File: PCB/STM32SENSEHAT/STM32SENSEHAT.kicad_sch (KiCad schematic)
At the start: 0 parts

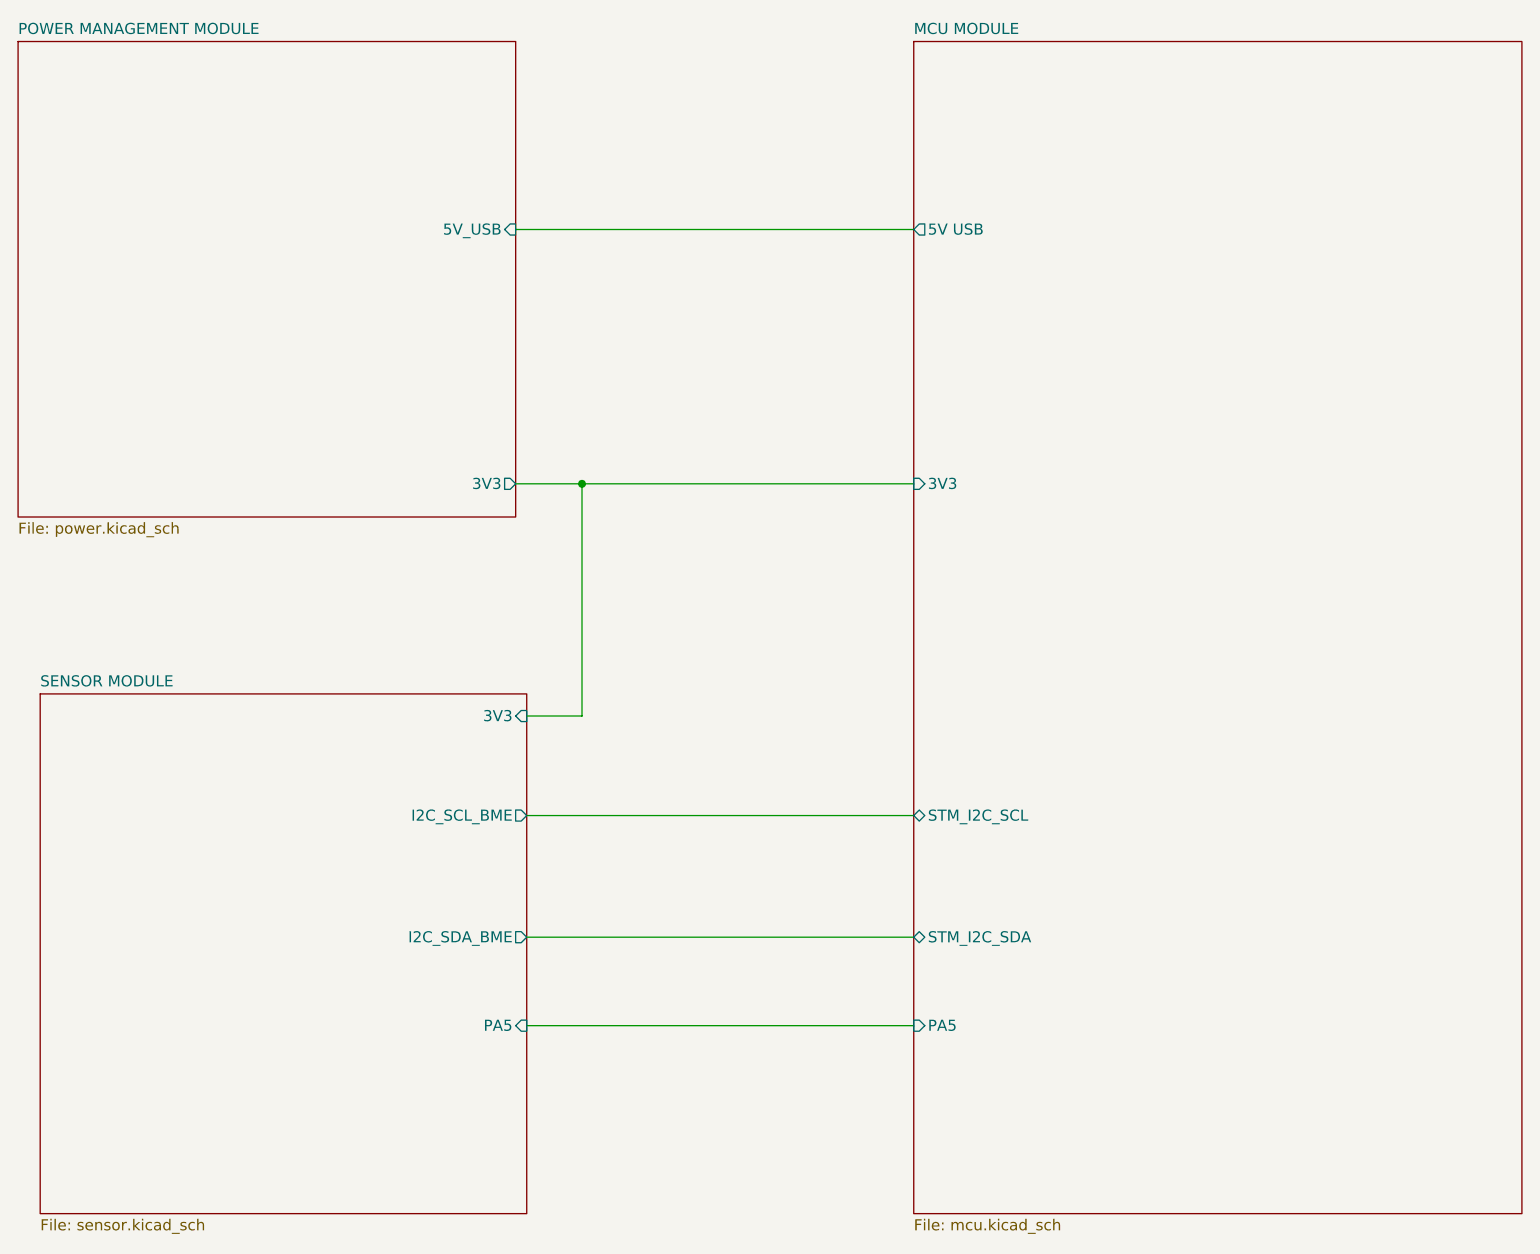
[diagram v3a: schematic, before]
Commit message: Added I2C,GPIO ports for the back up sesnors to the top level sheet
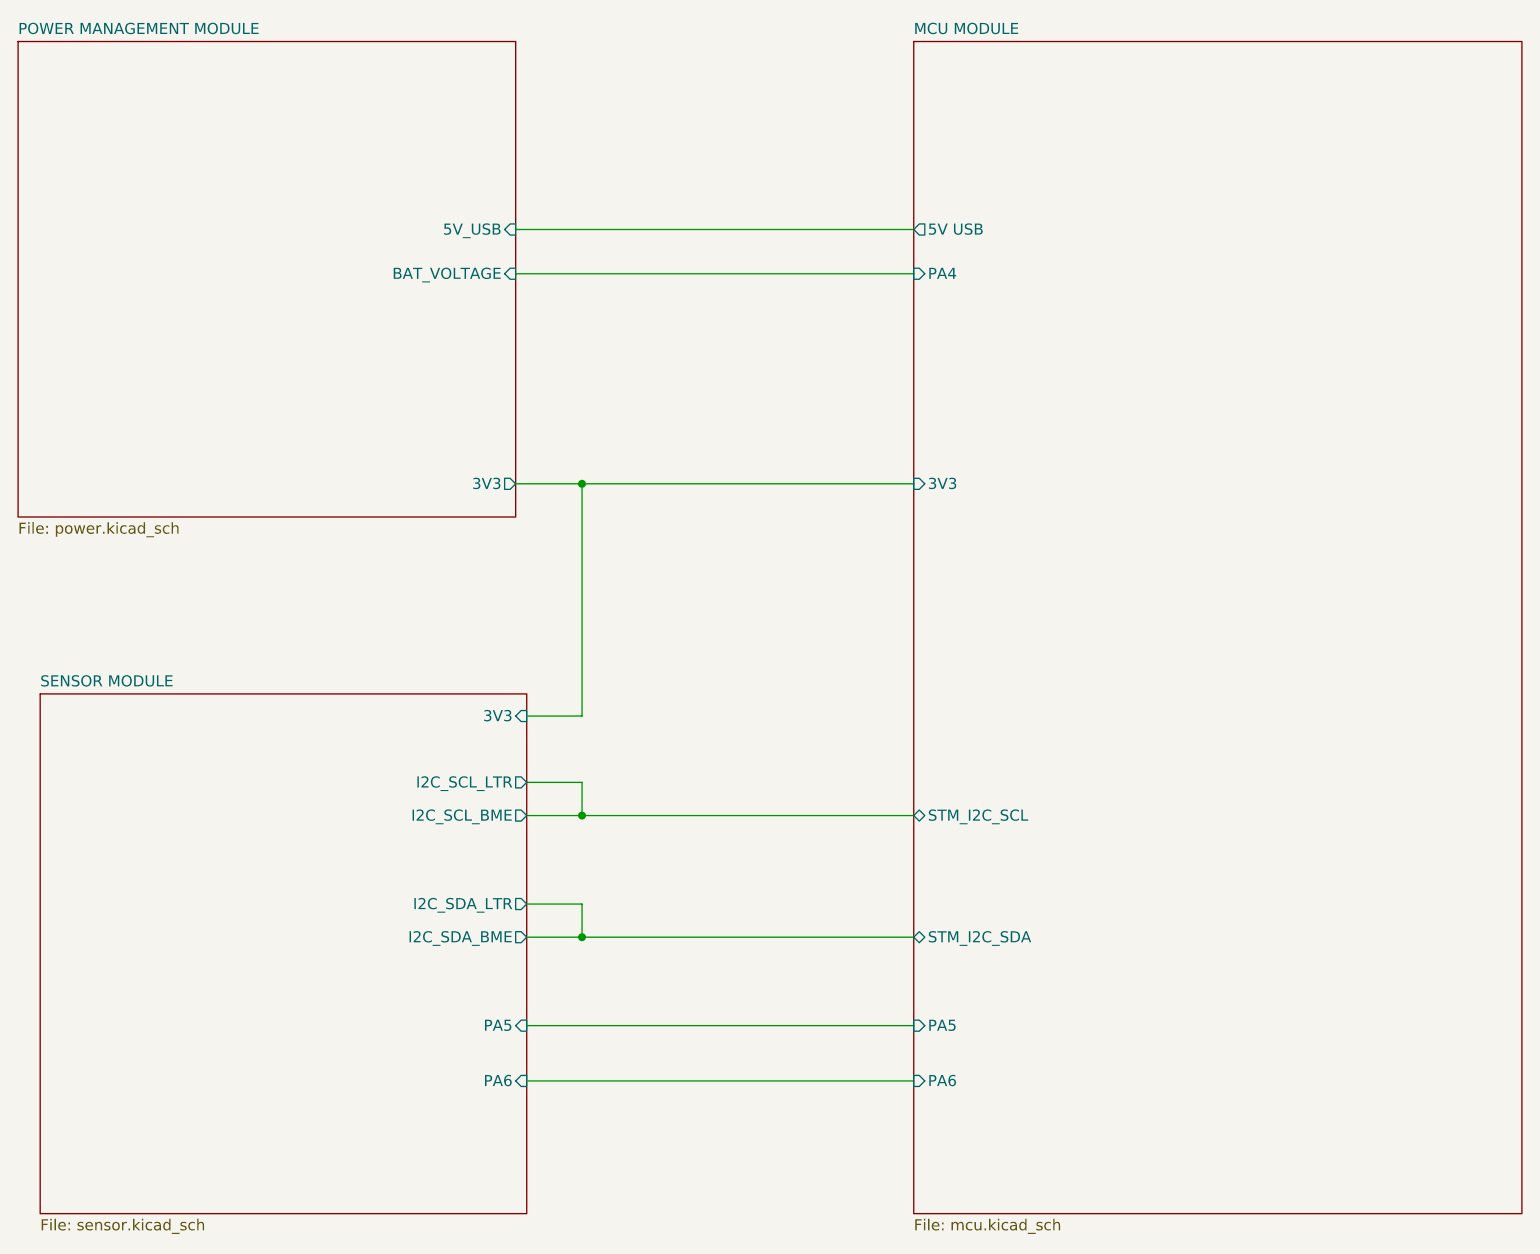
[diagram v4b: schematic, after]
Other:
- sheet MCU MODULE ports: added PA4, PA6; removed none
- sheet POWER MANAGEMENT MODULE ports: added BAT_VOLTAGE; removed none
- sheet SENSOR MODULE ports: added I2C_SCL_LTR, I2C_SDA_LTR, PA6; removed none
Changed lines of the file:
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@@
   (junction (at 99.06 73.66) (diameter 0) (color 0 0 0 0)
   )
+  (junction (at 99.06 125.73) (diameter 0) (color 0 0 0 0)
+  )
+  (junction (at 99.06 111.76) (diameter 0) (color 0 0 0 0)
+  )
+  (wire (pts (xy 92.71 142.24) (xy 137.16 142.24))
+    (stroke (width 0) (type default))
+  )
+  (wire (pts (xy 92.71 107.95) (xy 99.06 107.95))
+    (stroke (width 0) (type default))
+  )
+  (wire (pts (xy 99.06 111.76) (xy 137.16 111.76))
+    (stroke (width 0) (type default))
+  )
   (wire (pts (xy 91.44 73.66) (xy 99.06 73.66))
     (stroke (width 0) (type default))
@@
     (stroke (width 0) (type default))
   )
+  (wire (pts (xy 99.06 107.95) (xy 99.06 111.76))
+    (stroke (width 0) (type default))
+  )
   (wire (pts (xy 91.44 44.45) (xy 137.16 44.45))
     (stroke (width 0) (type default))
   )
-  (wire (pts (xy 92.71 125.73) (xy 137.16 125.73))
+  (wire (pts (xy 92.71 125.73) (xy 99.06 125.73))
+    (stroke (width 0) (type default))
+  )
+  (wire (pts (xy 99.06 121.92) (xy 99.06 125.73))
     (stroke (width 0) (type default))
   )
@@
     (stroke (width 0) (type default))
   )
-  (wire (pts (xy 92.71 111.76) (xy 137.16 111.76))
+  (wire (pts (xy 91.44 49.53) (xy 137.16 49.53))
+    (stroke (width 0) (type default))
+  )
+  (wire (pts (xy 92.71 111.76) (xy 99.06 111.76))
+    (stroke (width 0) (type default))
+  )
+  (wire (pts (xy 99.06 125.73) (xy 137.16 125.73))
+    (stroke (width 0) (type default))
+  )
+  (wire (pts (xy 92.71 121.92) (xy 99.06 121.92))
     (stroke (width 0) (type default))
   )
@@
       (effects (font (size 1.27 1.27)) (justify right))
     )
+    (pin "PA6" input (at 92.71 142.24 0)
+      (effects (font (size 1.27 1.27)) (justify right))
+    )
+    (pin "I2C_SCL_LTR" output (at 92.71 107.95 0)
+      (effects (font (size 1.27 1.27)) (justify right))
+    )
+    (pin "I2C_SDA_LTR" output (at 92.71 121.92 0)
+      (effects (font (size 1.27 1.27)) (justify right))
+    )
     (instances
       (project "STM32SENSEHAT"
@@
       (effects (font (size 1.27 1.27)) (justify left))
     )
+    (pin "PA6" input (at 137.16 142.24 180)
+      (effects (font (size 1.27 1.27)) (justify left))
+    )
+    (pin "PA4" input (at 137.16 49.53 180)
+      (effects (font (size 1.27 1.27)) (justify left))
+    )
     (instances
       (project "STM32SENSEHAT"
@@
       (effects (font (size 1.27 1.27)) (justify right))
     )
+    (pin "BAT_VOLTAGE" input (at 91.44 49.53 0)
+      (effects (font (size 1.27 1.27)) (justify right))
+    )

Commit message: Protectuion features added to all schematica
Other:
- sheet MCU MODULE ports: added none; removed 3V3, 5V USB, PA6
- sheet POWER MANAGEMENT MODULE ports: added none; removed 3V3, 5V_USB
- sheet SENSOR MODULE ports: added none; removed 3V3, PA6
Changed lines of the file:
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@@
     (comment 4 "AUTHOR(S)")
   )
-  (junction (at 99.06 73.66) (diameter 0) (color 0 0 0 0)
-  )
   (junction (at 99.06 125.73) (diameter 0) (color 0 0 0 0)
   )
   (junction (at 99.06 111.76) (diameter 0) (color 0 0 0 0)
-  )
-  (wire (pts (xy 92.71 142.24) (xy 137.16 142.24))
-    (stroke (width 0) (type default))
   )
   (wire (pts (xy 92.71 107.95) (xy 99.06 107.95))
@@
     (stroke (width 0) (type default))
   )
-  (wire (pts (xy 91.44 73.66) (xy 99.06 73.66))
-    (stroke (width 0) (type default))
-  )
-  (wire (pts (xy 99.06 73.66) (xy 137.16 73.66))
-    (stroke (width 0) (type default))
-  )
   (wire (pts (xy 99.06 107.95) (xy 99.06 111.76))
     (stroke (width 0) (type default))
   )
-  (wire (pts (xy 91.44 44.45) (xy 137.16 44.45))
-    (stroke (width 0) (type default))
-  )
   (wire (pts (xy 92.71 125.73) (xy 99.06 125.73))
     (stroke (width 0) (type default))
   )
   (wire (pts (xy 99.06 121.92) (xy 99.06 125.73))
-    (stroke (width 0) (type default))
-  )
-  (wire (pts (xy 92.71 100.33) (xy 99.06 100.33))
-    (stroke (width 0) (type default))
-  )
-  (wire (pts (xy 99.06 100.33) (xy 99.06 73.66))
     (stroke (width 0) (type default))
   )
@@
   (sheet (at 36.83 97.79) (size 55.88 59.69) (fields_autoplaced)
     (stroke (width 0.1524) (type solid))
-    (fill (color 255 255 255 1.0000))
+    (fill (color 0 255 0 1.0000))
     (property "Sheetname" "SENSOR MODULE" (at 36.83 97.0784 0)
       (effects (font (size 1.27 1.27)) (justify left bottom))
@@
       (effects (font (size 1.27 1.27)) (justify right))
     )
-    (pin "3V3" input (at 92.71 100.33 0)
-      (effects (font (size 1.27 1.27)) (justify right))
-    )
     (pin "I2C_SCL_BME" output (at 92.71 111.76 0)
-      (effects (font (size 1.27 1.27)) (justify right))
-    )
-    (pin "PA6" input (at 92.71 142.24 0)
       (effects (font (size 1.27 1.27)) (justify right))
     )
@@
   (sheet (at 137.16 22.86) (size 69.85 134.62) (fields_autoplaced)
     (stroke (width 0.1524) (type solid))
-    (fill (color 255 255 255 1.0000))
+    (fill (color 0 255 0 1.0000))
     (property "Sheetname" "MCU MODULE" (at 137.16 22.1484 0)
       (effects (font (size 1.27 1.27)) (justify left bottom))
@@
       (effects (font (size 1.27 1.27)) (justify left))
     )
-    (pin "3V3" input (at 137.16 73.66 180)
-      (effects (font (size 1.27 1.27)) (justify left))
-    )
-    (pin "5V USB" output (at 137.16 44.45 180)
-      (effects (font (size 1.27 1.27)) (justify left))
-    )
     (pin "STM_I2C_SCL" bidirectional (at 137.16 111.76 180)
       (effects (font (size 1.27 1.27)) (justify left))
     )
-    (pin "PA6" input (at 137.16 142.24 180)
-      (effects (font (size 1.27 1.27)) (justify left))
-    )
     (pin "PA4" input (at 137.16 49.53 180)
-      (effects (font (size 1.27 1.27)) (justify left))
+      (effects (font (size 1.27 1.27) (color 72 0 72 1)) (justify left))
     )
     (instances
@@
   (sheet (at 34.29 22.86) (size 57.15 54.61) (fields_autoplaced)
     (stroke (width 0.1524) (type solid))
-    (fill (color 255 255 255 1.0000))
+    (fill (color 0 255 0 1.0000))
     (property "Sheetname" "POWER MANAGEMENT MODULE" (at 34.29 22.1484 0)
       (effects (font (size 1.27 1.27)) (justify left bottom))
@@
       (effects (font (size 1.27 1.27)) (justify left top))
     )
-    (pin "3V3" output (at 91.44 73.66 0)
-      (effects (font (size 1.27 1.27)) (justify right))
-    )
-    (pin "5V_USB" input (at 91.44 44.45 0)
-      (effects (font (size 1.27 1.27)) (justify right))
-    )
     (pin "BAT_VOLTAGE" input (at 91.44 49.53 0)

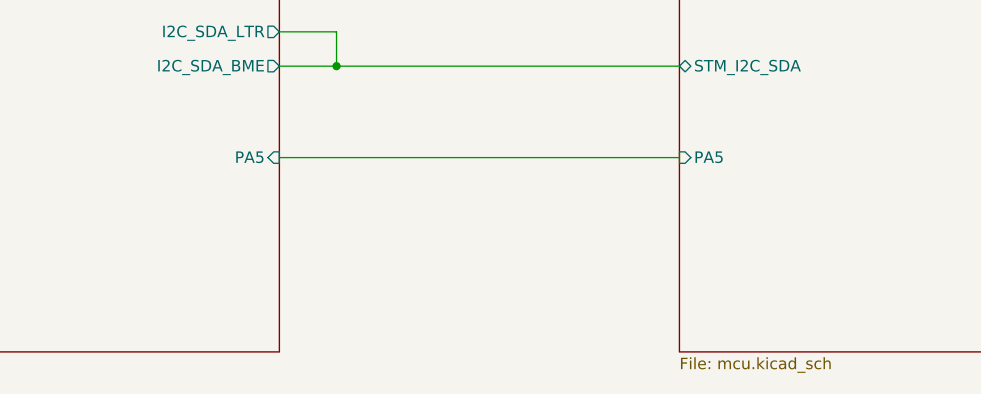
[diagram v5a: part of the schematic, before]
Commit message: Schematics review top sheet
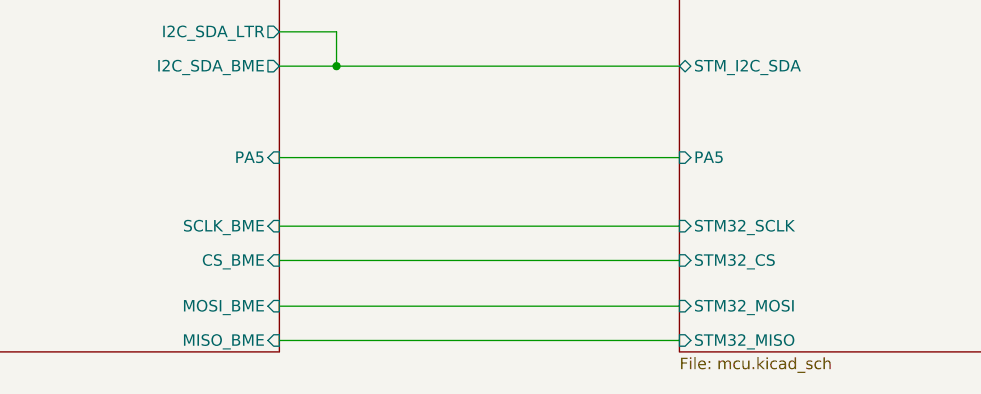
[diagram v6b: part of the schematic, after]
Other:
- sheet MCU MODULE ports: added STM32_CS, STM32_MISO, STM32_MOSI, STM32_SCLK; removed none
- sheet SENSOR MODULE ports: added CS_BME, MISO_BME, MOSI_BME, SCLK_BME; removed none
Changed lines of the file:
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@@
+    (stroke (width 0) (type default))
+  )
+  (wire (pts (xy 92.71 147.32) (xy 137.16 147.32))
     (stroke (width 0) (type default))
   )
@@
     (stroke (width 0) (type default))
   )
+  (wire (pts (xy 92.71 156.21) (xy 137.16 156.21))
+    (stroke (width 0) (type default))
+  )
   (wire (pts (xy 91.44 49.53) (xy 137.16 49.53))
     (stroke (width 0) (type default))
@@
     (stroke (width 0) (type default))
   )
+  (wire (pts (xy 92.71 143.51) (xy 137.16 143.51))
+    (stroke (width 0) (type default))
+  )
   (wire (pts (xy 99.06 125.73) (xy 137.16 125.73))
     (stroke (width 0) (type default))
@@
   )
   (wire (pts (xy 92.71 135.89) (xy 137.16 135.89))
+    (stroke (width 0) (type default))
+  )
+  (wire (pts (xy 92.71 152.4) (xy 137.16 152.4))
     (stroke (width 0) (type default))
   )
@@
       (effects (font (size 1.27 1.27)) (justify right))
     )
+    (pin "SCLK_BME" input (at 92.71 143.51 0)
+      (effects (font (size 1.27 1.27)) (justify right))
+    )
+    (pin "MISO_BME" input (at 92.71 156.21 0)
+      (effects (font (size 1.27 1.27)) (justify right))
+    )
+    (pin "CS_BME" input (at 92.71 147.32 0)
+      (effects (font (size 1.27 1.27)) (justify right))
+    )
+    (pin "MOSI_BME" input (at 92.71 152.4 0)
+      (effects (font (size 1.27 1.27)) (justify right))
+    )
     (instances
       (project "STM32SENSEHAT"
@@
       (effects (font (size 1.27 1.27) (color 72 0 72 1)) (justify left))
     )
+    (pin "STM32_SCLK" input (at 137.16 143.51 180)
+      (effects (font (size 1.27 1.27)) (justify left))
+    )
+    (pin "STM32_CS" input (at 137.16 147.32 180)
+      (effects (font (size 1.27 1.27)) (justify left))
+    )
+    (pin "STM32_MOSI" input (at 137.16 152.4 180)
+      (effects (font (size 1.27 1.27)) (justify left))
+    )
+    (pin "STM32_MISO" input (at 137.16 156.21 180)
+      (effects (font (size 1.27 1.27)) (justify left))
+    )
     (instances
